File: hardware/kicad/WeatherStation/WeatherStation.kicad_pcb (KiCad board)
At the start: 4 copper layers, 100 x 80 mm, 7 parts

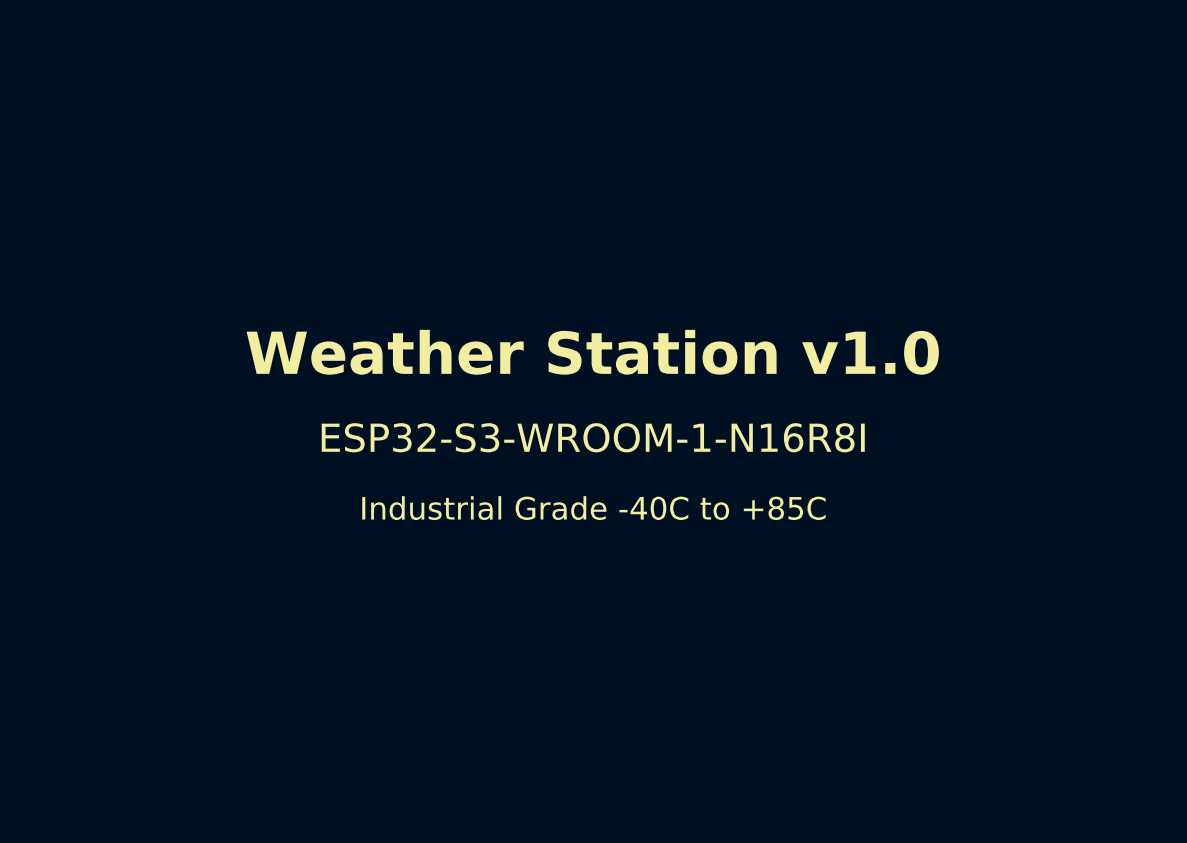
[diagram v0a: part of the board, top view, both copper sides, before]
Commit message: Add P9E Microsystems branding to board markings
Front silkscreen: P9E (bold), P9E Microsystems Pvt Ltd, www.p9e.in
Back silkscreen: P9E Microsystems Pvt Ltd + www.p9e.in added
Title blocks: company updated to P9E Microsystems Pvt Ltd
Also updated PCB title/rev/date for STM32F407 v2.0

https://claude.ai/code/session_01XHnfZQ5BbxTCTBMCteQyVe
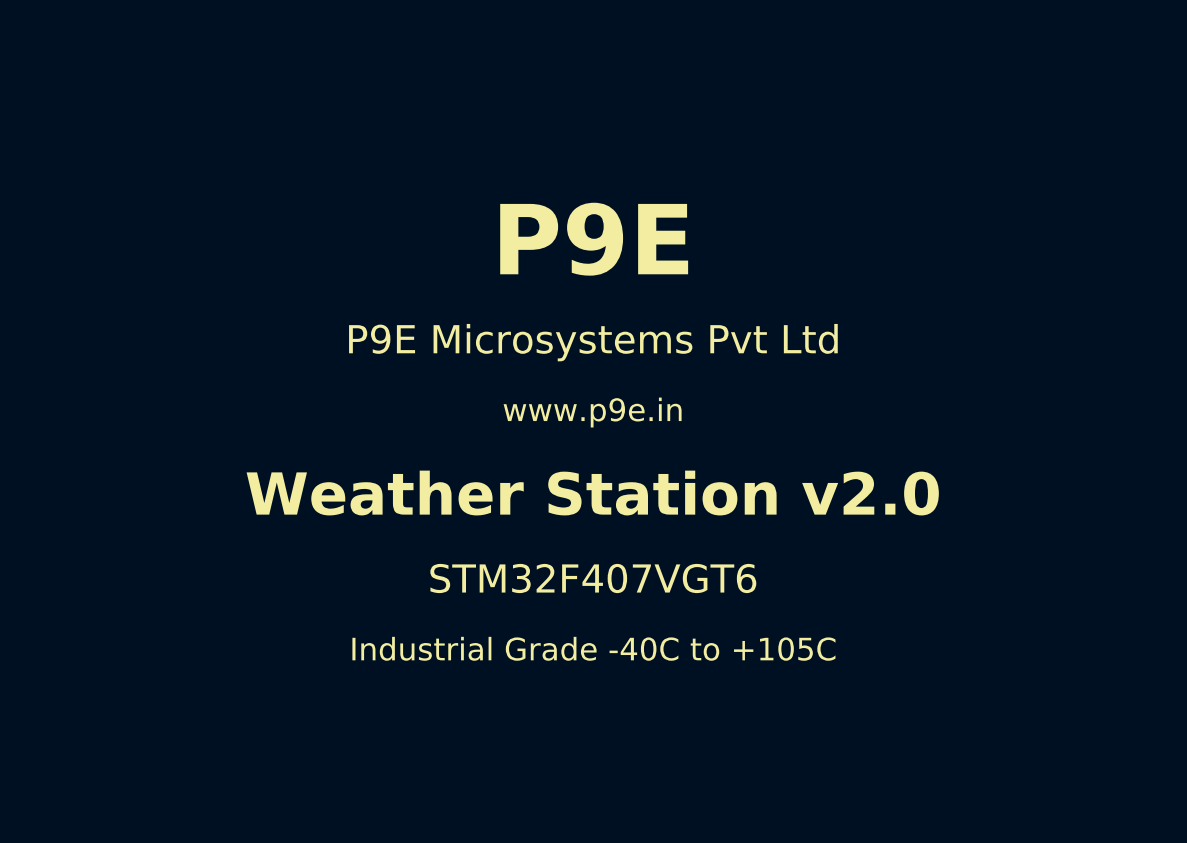
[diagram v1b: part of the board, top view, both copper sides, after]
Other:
- board text added: "Industrial Grade -40C to +105C"
- board text added: "P9E"
- board text added: "P9E Microsystems Pvt Ltd"
- board text added: "P9E Microsystems Pvt Ltd www.p9e.in Weather Station PCB Rev 2.0 Designed for outdoor deployment Apply conformal coating before use RoHS Compliant"
- board text added: "STM32F407VGT6"
- board text added: "Weather Station v2.0"
- board text added: "www.p9e.in"
- board text removed: "ESP32-S3-WROOM-1-N16R8I"
- board text removed: "Industrial Grade -40C to +85C"
- board text removed: "Weather Station PCB Rev 1.0 Designed for outdoor deployment Apply conformal coating before use RoHS Compliant"
- board text removed: "Weather Station v1.0"
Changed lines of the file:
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@@
   (paper "A4")
   (title_block
-    (title "ESP32-S3 Weather Station PCB")
-    (date "2026-02-28")
-    (rev "1.0")
-    (company "Weather Station Project")
+    (title "STM32F407 Weather Station PCB")
+    (date "2026-03-19")
+    (rev "2.0")
+    (company "P9E Microsystems Pvt Ltd")
     (comment 1 "4-layer PCB, 1.6mm, ENIG finish")
     (comment 2 "Industrial outdoor weather monitoring")
-    (comment 3 "ESP32-S3-WROOM-1-N16R8I")
+    (comment 3 "STM32F407VGT6 Single-MCU")
     (comment 4 "FR4 Tg170, IPC Class 2")
   )
@@
   ;; SILKSCREEN LABELS
   ;; =====================================================================
-  (gr_text "Weather Station v1.0" (at 50 40) (layer "F.SilkS")
+  (gr_text "P9E" (at 50 36) (layer "F.SilkS")
+    (effects (font (size 2.5 2.5) (thickness 0.3) (bold yes)) (justify center))
+  )
+  (gr_text "P9E Microsystems Pvt Ltd" (at 50 39.5) (layer "F.SilkS")
+    (effects (font (size 1 1) (thickness 0.15)) (justify center))
+  )
+  (gr_text "www.p9e.in" (at 50 42) (layer "F.SilkS")
+    (effects (font (size 0.8 0.8) (thickness 0.12)) (justify center))
+  )
+  (gr_text "Weather Station v2.0" (at 50 45) (layer "F.SilkS")
     (effects (font (size 1.5 1.5) (thickness 0.2) (bold yes)) (justify center))
   )
-  (gr_text "ESP32-S3-WROOM-1-N16R8I" (at 50 43) (layer "F.SilkS")
+  (gr_text "STM32F407VGT6" (at 50 48) (layer "F.SilkS")
     (effects (font (size 1 1) (thickness 0.15)) (justify center))
   )
-  (gr_text "Industrial Grade -40C to +85C" (at 50 45.5) (layer "F.SilkS")
+  (gr_text "Industrial Grade -40C to +105C" (at 50 50.5) (layer "F.SilkS")
     (effects (font (size 0.8 0.8) (thickness 0.12)) (justify center))
   )
-  ;; Back silkscreen: pin labels and regulatory marks
-  (gr_text "Weather Station PCB Rev 1.0\nDesigned for outdoor deployment\nApply conformal coating before use\nRoHS Compliant" (at 50 40) (layer "B.SilkS")
+  ;; Back silkscreen: manufacturer info and regulatory marks
+  (gr_text "P9E Microsystems Pvt Ltd\nwww.p9e.in\nWeather Station PCB Rev 2.0\nDesigned for outdoor deployment\nApply conformal coating before use\nRoHS Compliant" (at 50 40) (layer "B.SilkS")
     (effects (font (size 1 1) (thickness 0.15)) (justify center mirror))
   )

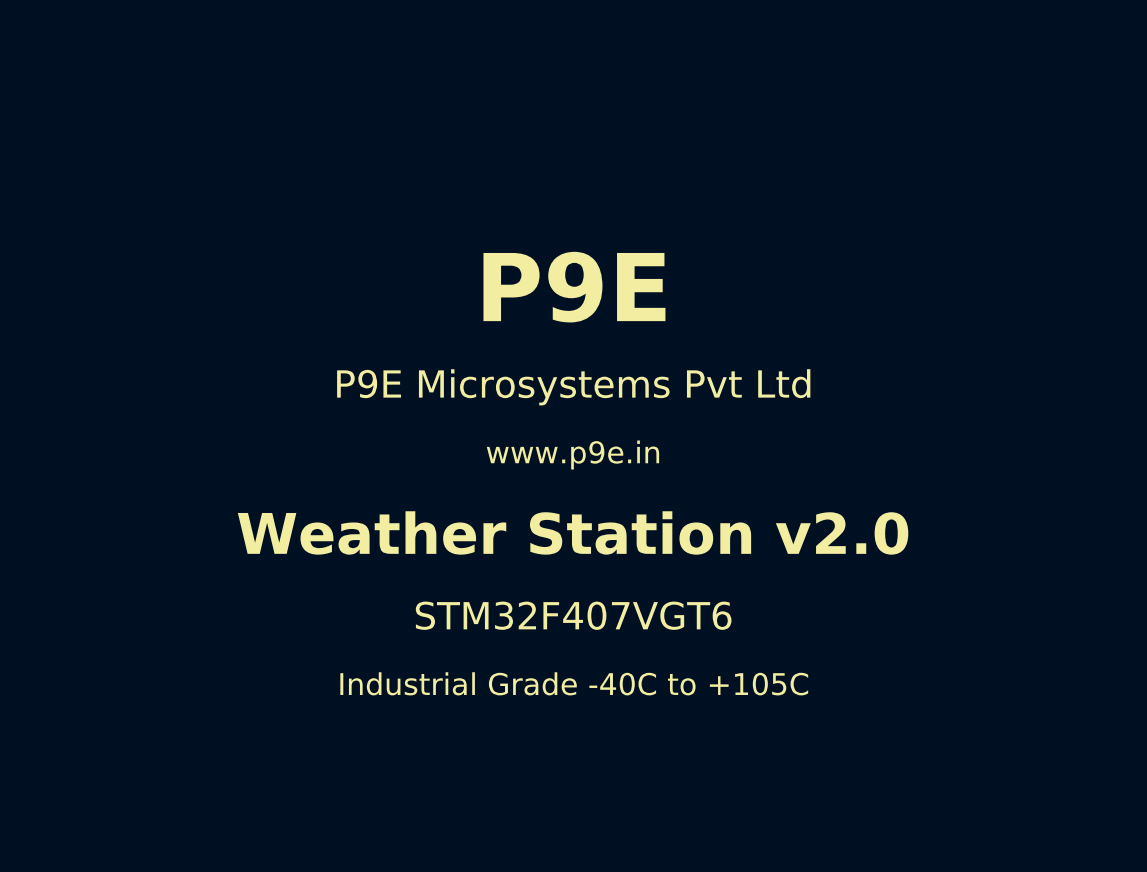
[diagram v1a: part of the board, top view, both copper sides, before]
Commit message: style: apply P9E 3-line label format on front and back silkscreen
Front silkscreen (F.SilkS) — 3-line P9E label block:
  Line 1: P9E              (3.5mm bold, company mark)
  Line 2: P9E Microsystems Pvt Ltd  (1.2mm bold, full name)
  Line 3: www.p9e.in       (1.0mm, website)

Product info kept separate below the label block:
  Weather Station v2.0 | STM32F407VGT6 | Industrial -40C/+105C

Back silkscreen (B.SilkS) — matching 3-line P9E label:
  P9E / P9E Microsystems Pvt Ltd / www.p9e.in
  Plus regulatory info: Rev 2.0, 4-Layer, ENIG, RoHS, IPC Class 2

Applied consistently to both WeatherStation.kicad_pcb (outline)
and WeatherStation_mfg.kicad_pcb (manufacturing).

https://claude.ai/code/session_01XHnfZQ5BbxTCTBMCteQyVe
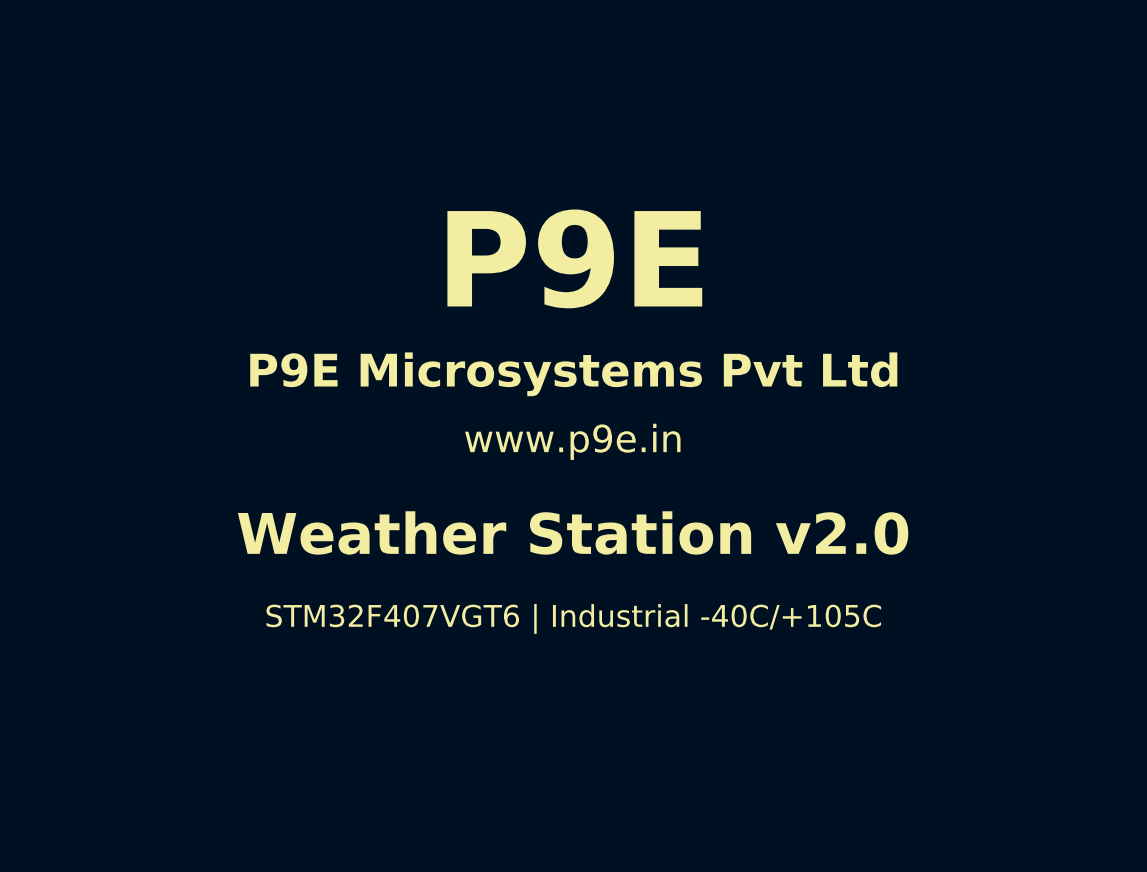
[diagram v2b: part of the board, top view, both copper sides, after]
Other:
- board text added: "P9E P9E Microsystems Pvt Ltd www.p9e.in"
- board text added: "STM32F407VGT6 | Industrial -40C/+105C"
- board text added: "Weather Station PCB Rev 2.0 4-Layer | FR4 Tg170 | ENIG RoHS Compliant | IPC Class 2 Conformal coat before deployment"
- board text removed: "Industrial Grade -40C to +105C"
- board text removed: "P9E Microsystems Pvt Ltd www.p9e.in Weather Station PCB Rev 2.0 Designed for outdoor deployment Apply conformal coating before use RoHS Compliant"
- board text removed: "STM32F407VGT6"
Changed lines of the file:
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@@
   ;; SILKSCREEN LABELS
   ;; =====================================================================
-  (gr_text "P9E" (at 50 36) (layer "F.SilkS")
-    (effects (font (size 2.5 2.5) (thickness 0.3) (bold yes)) (justify center))
+  ;; P9E 3-Line Label — Front silkscreen (centered on board)
+  (gr_text "P9E" (at 50 35) (layer "F.SilkS")
+    (effects (font (size 3.5 3.5) (thickness 0.4) (bold yes)) (justify center))
   )
-  (gr_text "P9E Microsystems Pvt Ltd" (at 50 39.5) (layer "F.SilkS")
+  (gr_text "P9E Microsystems Pvt Ltd" (at 50 39) (layer "F.SilkS")
+    (effects (font (size 1.2 1.2) (thickness 0.18) (bold yes)) (justify center))
+  )
+  (gr_text "www.p9e.in" (at 50 41.5) (layer "F.SilkS")
     (effects (font (size 1 1) (thickness 0.15)) (justify center))
   )
-  (gr_text "www.p9e.in" (at 50 42) (layer "F.SilkS")
-    (effects (font (size 0.8 0.8) (thickness 0.12)) (justify center))
-  )
+  ;; Product info (below P9E label)
   (gr_text "Weather Station v2.0" (at 50 45) (layer "F.SilkS")
     (effects (font (size 1.5 1.5) (thickness 0.2) (bold yes)) (justify center))
   )
-  (gr_text "STM32F407VGT6" (at 50 48) (layer "F.SilkS")
-    (effects (font (size 1 1) (thickness 0.15)) (justify center))
-  )
-  (gr_text "Industrial Grade -40C to +105C" (at 50 50.5) (layer "F.SilkS")
+  (gr_text "STM32F407VGT6 | Industrial -40C/+105C" (at 50 48) (layer "F.SilkS")
     (effects (font (size 0.8 0.8) (thickness 0.12)) (justify center))
   )
-  ;; Back silkscreen: manufacturer info and regulatory marks
-  (gr_text "P9E Microsystems Pvt Ltd\nwww.p9e.in\nWeather Station PCB Rev 2.0\nDesigned for outdoor deployment\nApply conformal coating before use\nRoHS Compliant" (at 50 40) (layer "B.SilkS")
+  ;; P9E 3-Line Label — Back silkscreen
+  (gr_text "P9E\nP9E Microsystems Pvt Ltd\nwww.p9e.in" (at 50 35) (layer "B.SilkS")
+    (effects (font (size 1.5 1.5) (thickness 0.2) (bold yes)) (justify center mirror))
+  )
+  ;; Back silkscreen — regulatory/specs
+  (gr_text "Weather Station PCB Rev 2.0\n4-Layer | FR4 Tg170 | ENIG\nRoHS Compliant | IPC Class 2\nConformal coat before deployment" (at 50 44) (layer "B.SilkS")
     (effects (font (size 1 1) (thickness 0.15)) (justify center mirror))
   )
